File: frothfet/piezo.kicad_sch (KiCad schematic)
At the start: 4 parts, among them Q11 AO3400A

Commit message: added test points
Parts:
- renumbered R57 to R48, R58 to R49
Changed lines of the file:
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@@
 		(dnp no)
 		(fields_autoplaced yes)
-		(property "Reference" "R58"
+		(property "Reference" "R49"
 			(at 127 104.1399 0)
 			(effects
@@
 			(project "frothfet"
 				(path "/c83c6236-96e9-46ad-9d7a-9e2efa4a7966/13bd1484-e1d0-414c-b70b-256f3904dbbc"
-					(reference "R58")
+					(reference "R49")
 					(unit 1)
 				)
@@
 		(dnp no)
 		(fields_autoplaced yes)
-		(property "Reference" "R57"
+		(property "Reference" "R48"
 			(at 119.38 93.98 90)
 			(effects
@@
 			(project "frothfet"
 				(path "/c83c6236-96e9-46ad-9d7a-9e2efa4a7966/13bd1484-e1d0-414c-b70b-256f3904dbbc"
-					(reference "R57")
+					(reference "R48")
 					(unit 1)
 				)
@@
 		(dnp no)
 		(fields_autoplaced yes)
-		(property "Reference" "#PWR0135"
+		(property "Reference" "#PWR0132"
 			(at 134.62 76.2 0)
 			(effects
@@
 			(project "frothfet"
 				(path "/c83c6236-96e9-46ad-9d7a-9e2efa4a7966/13bd1484-e1d0-414c-b70b-256f3904dbbc"
-					(reference "#PWR0135")
+					(reference "#PWR0132")
 					(unit 1)
 				)
@@
 		(dnp no)
 		(fields_autoplaced yes)
-		(property "Reference" "#PWR136"
+		(property "Reference" "#PWR0133"
 			(at 134.62 115.57 0)
 			(effects
@@
 			(project "frothfet"
 				(path "/c83c6236-96e9-46ad-9d7a-9e2efa4a7966/13bd1484-e1d0-414c-b70b-256f3904dbbc"
-					(reference "#PWR136")
-					(unit 1)
-				)
+					(reference "#PWR0133")
+					(unit 1)
+				)

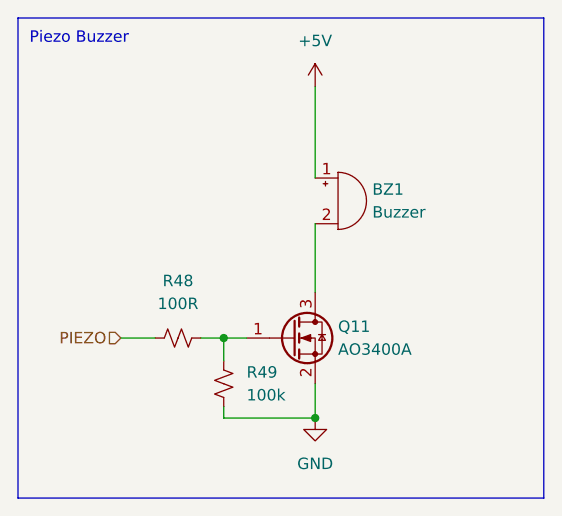
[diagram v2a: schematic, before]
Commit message: channel routing is basically done
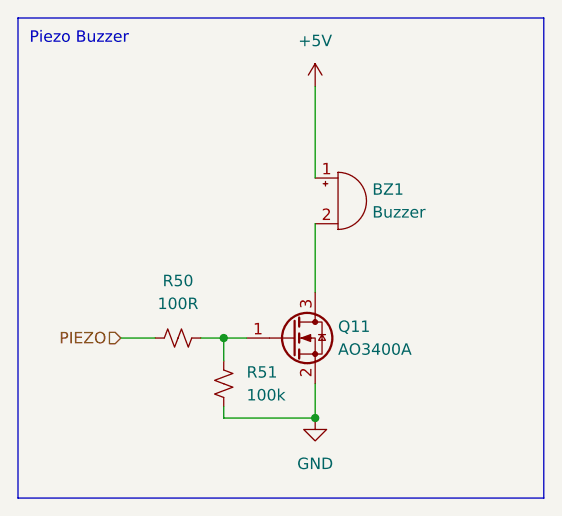
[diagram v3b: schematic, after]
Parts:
- renumbered R48 to R50, R49 to R51
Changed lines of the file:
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@@
 		(dnp no)
 		(fields_autoplaced yes)
-		(property "Reference" "R49"
+		(property "Reference" "R51"
 			(at 127 104.1399 0)
 			(effects
@@
 			(project "frothfet"
 				(path "/c83c6236-96e9-46ad-9d7a-9e2efa4a7966/13bd1484-e1d0-414c-b70b-256f3904dbbc"
-					(reference "R49")
+					(reference "R51")
 					(unit 1)
 				)
@@
 		(dnp no)
 		(fields_autoplaced yes)
-		(property "Reference" "R48"
+		(property "Reference" "R50"
 			(at 119.38 93.98 90)
 			(effects
@@
 			(project "frothfet"
 				(path "/c83c6236-96e9-46ad-9d7a-9e2efa4a7966/13bd1484-e1d0-414c-b70b-256f3904dbbc"
-					(reference "R48")
+					(reference "R50")
 					(unit 1)
 				)

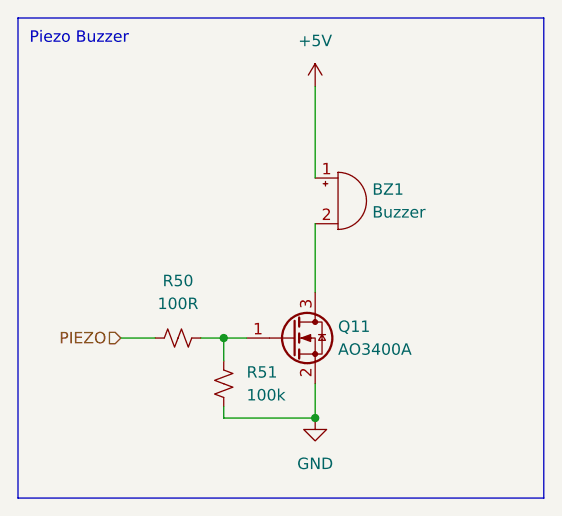
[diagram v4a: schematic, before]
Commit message: added more esd protection to 3.3v and 5v rails.
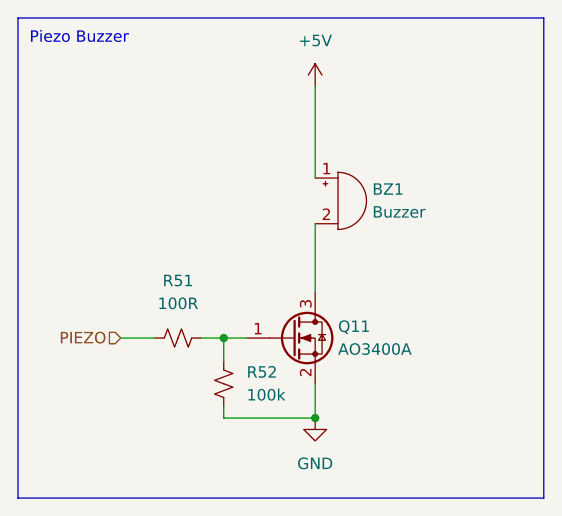
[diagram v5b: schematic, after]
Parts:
- renumbered R50 to R51, R51 to R52
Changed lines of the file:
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@@
 		(dnp no)
 		(fields_autoplaced yes)
-		(property "Reference" "R51"
+		(property "Reference" "R52"
 			(at 127 104.1399 0)
 			(effects
@@
 			(project "frothfet"
 				(path "/c83c6236-96e9-46ad-9d7a-9e2efa4a7966/13bd1484-e1d0-414c-b70b-256f3904dbbc"
-					(reference "R51")
+					(reference "R52")
 					(unit 1)
 				)
@@
 		(dnp no)
 		(fields_autoplaced yes)
-		(property "Reference" "R50"
+		(property "Reference" "R51"
 			(at 119.38 93.98 90)
 			(effects
@@
 			(project "frothfet"
 				(path "/c83c6236-96e9-46ad-9d7a-9e2efa4a7966/13bd1484-e1d0-414c-b70b-256f3904dbbc"
-					(reference "R50")
+					(reference "R51")
 					(unit 1)
 				)
@@
 		(dnp no)
 		(fields_autoplaced yes)
-		(property "Reference" "#PWR0139"
+		(property "Reference" "#PWR0149"
 			(at 134.62 76.2 0)
 			(effects
@@
 			(project "frothfet"
 				(path "/c83c6236-96e9-46ad-9d7a-9e2efa4a7966/13bd1484-e1d0-414c-b70b-256f3904dbbc"
-					(reference "#PWR0139")
+					(reference "#PWR0149")
 					(unit 1)
 				)
@@
 		(dnp no)
 		(fields_autoplaced yes)
-		(property "Reference" "#PWR0140"
+		(property "Reference" "#PWR0150"
 			(at 134.62 115.57 0)
 			(effects
@@
 			(project "frothfet"
 				(path "/c83c6236-96e9-46ad-9d7a-9e2efa4a7966/13bd1484-e1d0-414c-b70b-256f3904dbbc"
-					(reference "#PWR0140")
-					(unit 1)
-				)
+					(reference "#PWR0150")
+					(unit 1)
+				)

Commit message: added support for ALERT pin from INA226 for overcurrent protection (hopefully)
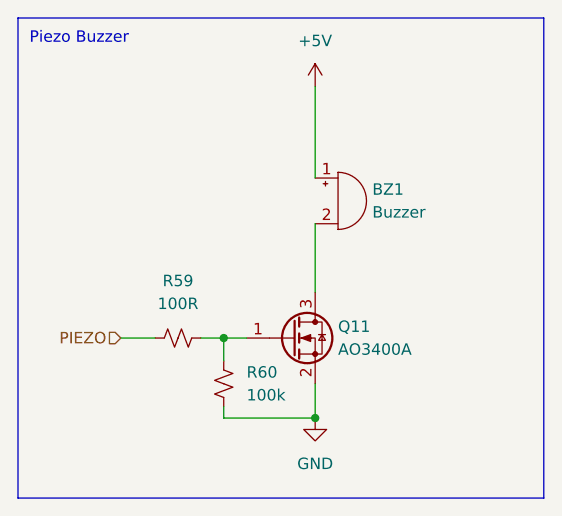
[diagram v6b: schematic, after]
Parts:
- renumbered R51 to R59, R52 to R60
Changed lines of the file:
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@@
 		(dnp no)
 		(fields_autoplaced yes)
-		(property "Reference" "R52"
+		(property "Reference" "R60"
 			(at 127 104.1399 0)
 			(effects
@@
 			(project "frothfet"
 				(path "/c83c6236-96e9-46ad-9d7a-9e2efa4a7966/13bd1484-e1d0-414c-b70b-256f3904dbbc"
-					(reference "R52")
+					(reference "R60")
 					(unit 1)
 				)
@@
 		(dnp no)
 		(fields_autoplaced yes)
-		(property "Reference" "R51"
+		(property "Reference" "R59"
 			(at 119.38 93.98 90)
 			(effects
@@
 			(project "frothfet"
 				(path "/c83c6236-96e9-46ad-9d7a-9e2efa4a7966/13bd1484-e1d0-414c-b70b-256f3904dbbc"
-					(reference "R51")
+					(reference "R59")
 					(unit 1)
 				)
